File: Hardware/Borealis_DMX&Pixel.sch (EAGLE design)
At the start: 9 parts, among them IC2 SP3485, J1 RJ45-854602-908LF

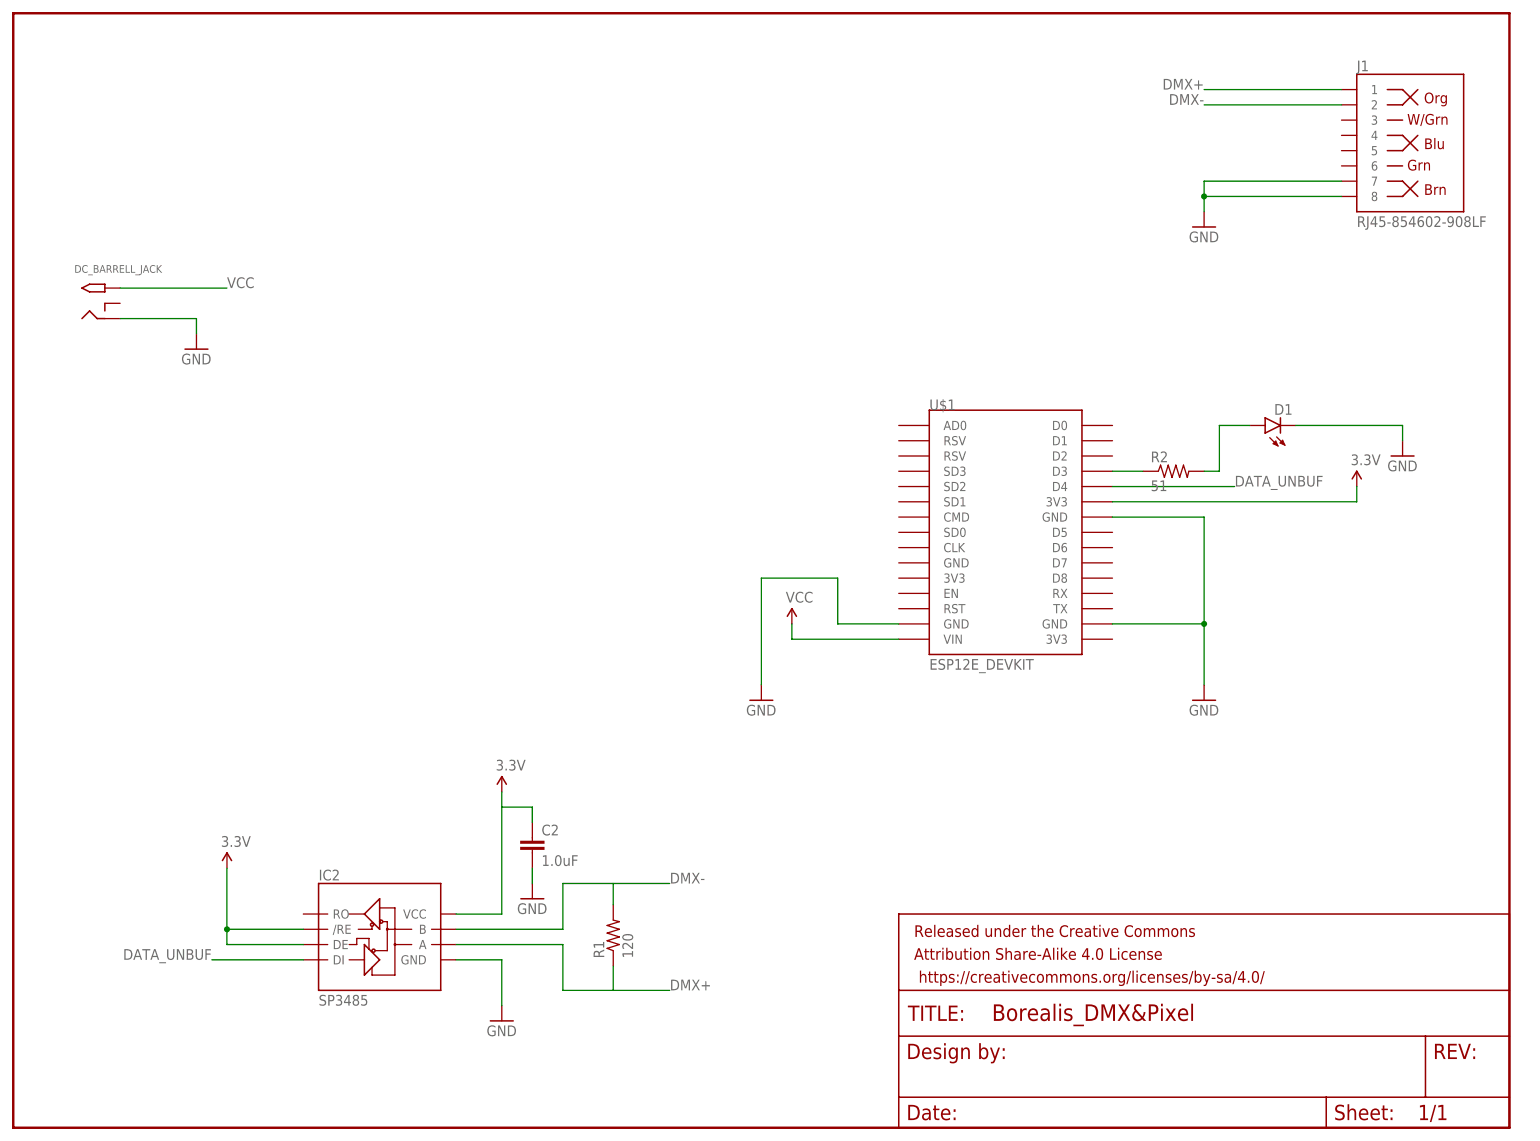
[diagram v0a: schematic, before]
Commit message: Replaced erroneously committed DMX only output design files with DMX & Pixel version refrenced in repo documentation.
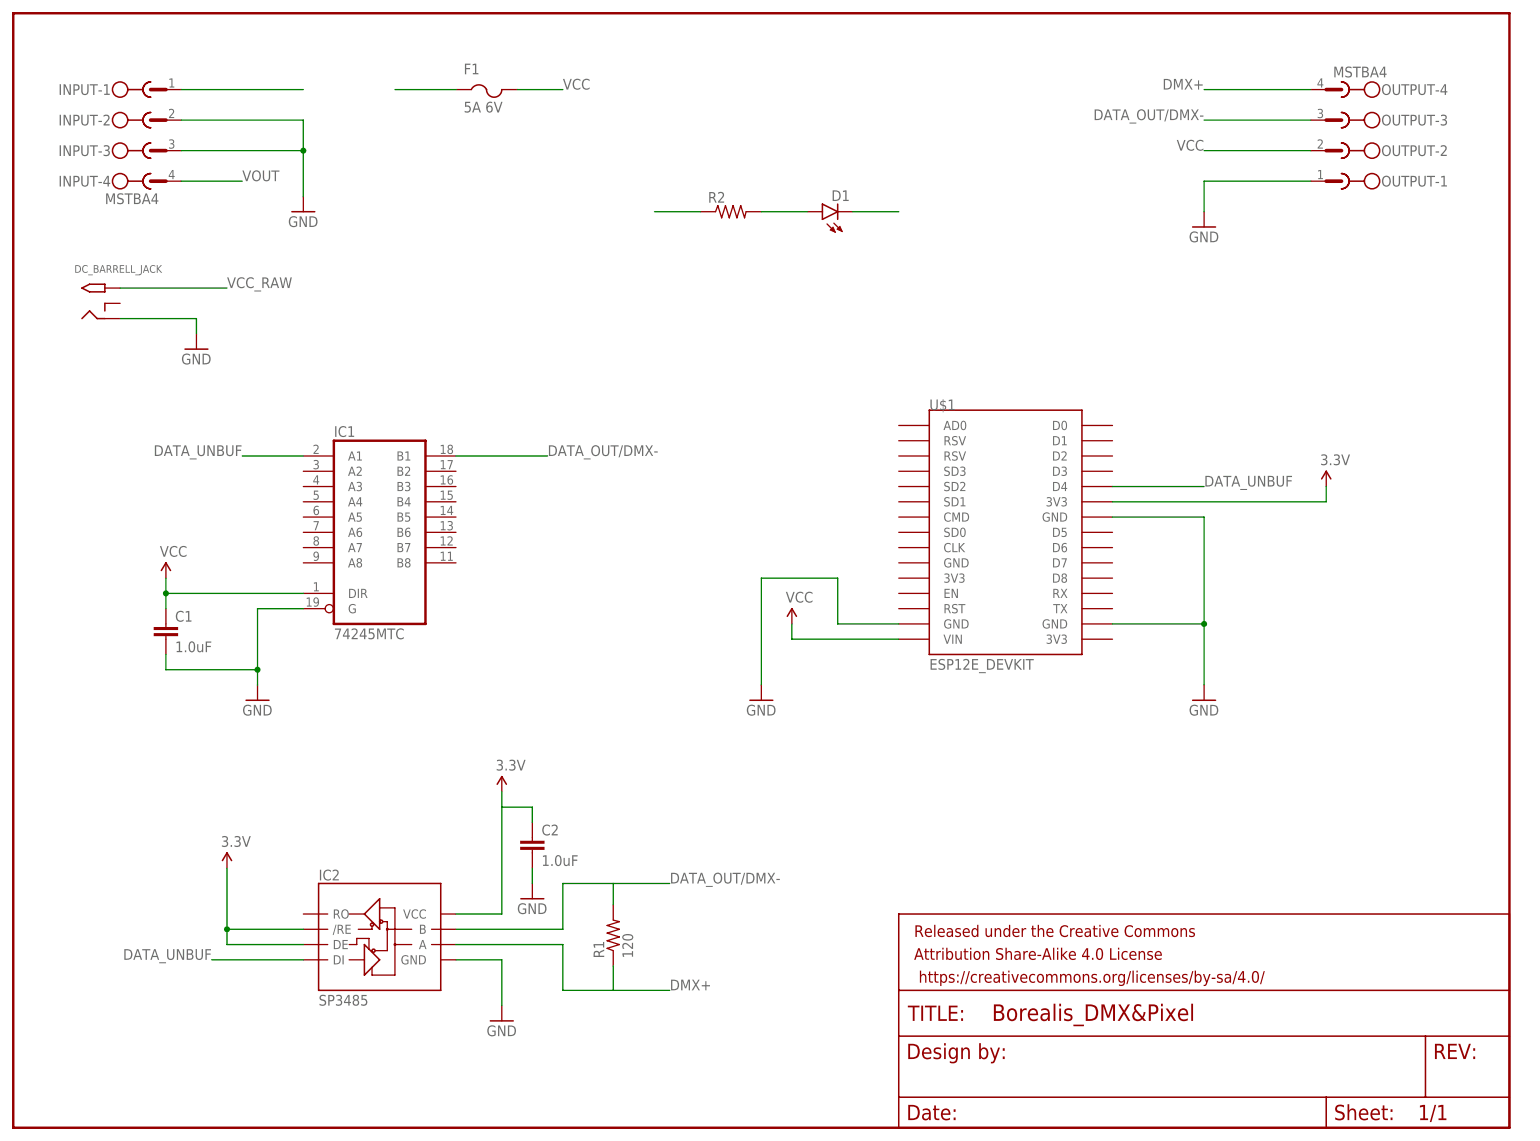
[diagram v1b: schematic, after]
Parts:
- removed J1: RJ45-854602-908LF, SparkFun-Connectors:RJ45-854602-908LF
- added C1: 1.0uF, SparkFun-Capacitors:1.0UF-16V-10%(0603)
- added F1: 5A 6V, adafruit:PTCFUSE-1206
- added IC1: 74245MTC, adafruit:74245MTC
- added INPUT, OUTPUT: MSTBA4, con-phoenix-508:MSTBA4
- R2: value 51 -> (none)
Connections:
- removed net DMX-: IC2.B, J1.2, R1.2
- removed net N$1: R2.1, U$1.D3
- new net DATA_OUT/DMX-: IC1A.B1, IC2.B, OUTPUT-3.1, R1.2
- new net VCC_RAW: DC_BARRELL_JACK.TIP, F1.1, INPUT-1.1
- new net VOUT: INPUT-4.1
- net DATA_UNBUF: now also IC1A.A1
- net DMX+: now also OUTPUT-4.1; no longer J1.1
- net GND: now also C1.2, IC1A.G, INPUT-2.1, INPUT-3.1, OUTPUT-1.1; no longer J1.7, J1.8
- net VCC: now also C1.1, F1.2, IC1A.DIR, OUTPUT-2.1, R2.1; no longer DC_BARRELL_JACK.TIP
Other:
- moved on the sheet: D1, R2
